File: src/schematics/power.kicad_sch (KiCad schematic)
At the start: 43 parts, among them U1 L6981NDR, U2 L6981NDR, U3 ST1S41PHR, U4 L6981NDR, U5 LM3880

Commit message: Adds footprint for etq-p5m220yfc (#64)
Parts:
- L2, L4: footprint (none) -> ECAP5-DPROC:ETQ-P5M220YFC
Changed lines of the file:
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@@
 			)
 		)
-		(property "Footprint" ""
+		(property "Footprint" "ECAP5-DPROC:ETQ-P5M220YFC"
 			(at 240.03 34.29 0)
 			(effects
@@
 			)
 		)
-		(property "Footprint" ""
+		(property "Footprint" "ECAP5-DPROC:ETQ-P5M220YFC"
 			(at 240.03 85.09 0)
 			(effects

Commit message: Adds footprint for ETQ-P3M2R2KVP (#65)
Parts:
- L3: footprint (none) -> ECAP5-DPROC:ETQ-P3M2R2KVP
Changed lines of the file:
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@@
 			)
 		)
-		(property "Footprint" ""
+		(property "Footprint" "ECAP5-DPROC:ETQ-P3M2R2KVP"
 			(at 104.14 85.09 0)
 			(effects

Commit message: Add footprint for st1s41phr
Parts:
- U3: footprint (none) -> ECAP5-DPROC:ST1S41PHR
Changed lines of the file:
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@@
 			)
 		)
-		(property "Footprint" ""
+		(property "Footprint" "ECAP5-DPROC:ST1S41PHR"
 			(at 88.265 100.33 0)
 			(effects

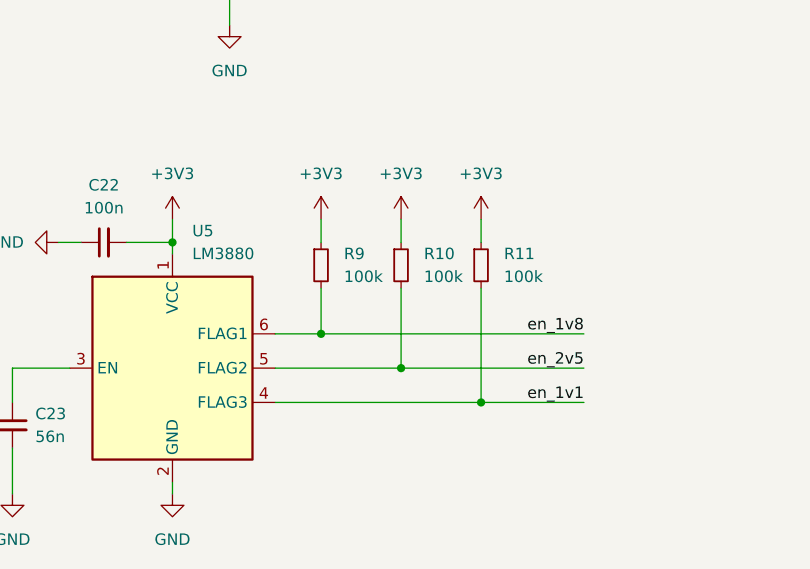
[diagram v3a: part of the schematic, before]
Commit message: Adds footprint for lm3880 (#67)
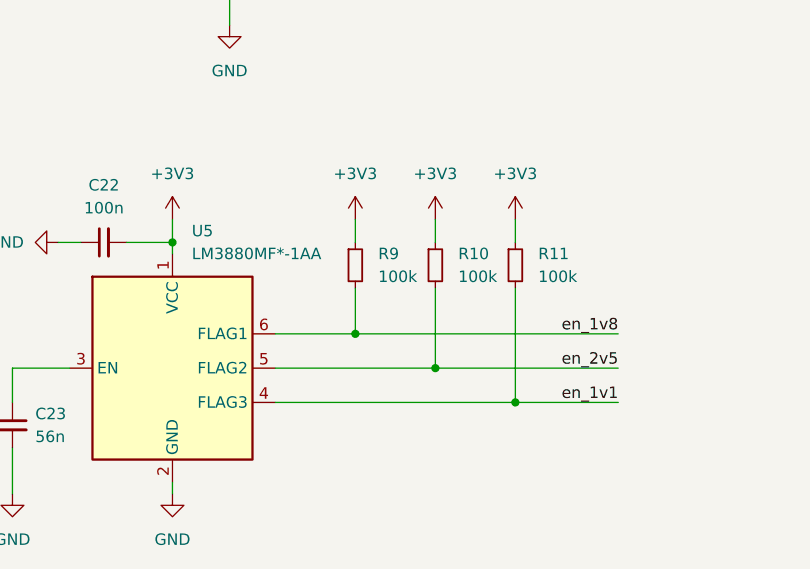
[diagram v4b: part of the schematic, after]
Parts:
- U5: value LM3880 -> LM3880MF*-1AA; footprint (none) -> ECAP5-DPROC:LM3880
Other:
- moved on the sheet: R10, R11, R9

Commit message: Add remaining component footprints (#79)
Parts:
- C1, C13, C14, C2, C22, C23, C3, C4: footprint (none) -> Capacitor_SMD:C_0402_1005Metric
- C11, C12, C16, C20, C21, C8, C9: footprint (none) -> Capacitor_SMD:C_0603_1608Metric
- C5: footprint Capacitor_SMD:C_1210_3225Metric -> Capacitor_SMD:C_0805_2012Metric
- R1, R10, R11, R2, R3, R4, R5, R6, R7, R8, R9: footprint (none) -> Resistor_SMD:R_0603_1608Metric
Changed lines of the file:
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@@
 			)
 		)
-		(property "Footprint" ""
+		(property "Footprint" "Resistor_SMD:R_0603_1608Metric"
 			(at 110.49 90.17 0)
 			(effects
@@
 			)
 		)
-		(property "Footprint" ""
+		(property "Footprint" "Capacitor_SMD:C_0402_1005Metric"
 			(at 60.96 153.67 0)
 			(effects
@@
 			)
 		)
-		(property "Footprint" ""
+		(property "Footprint" "Resistor_SMD:R_0603_1608Metric"
 			(at 250.19 90.17 0)
 			(effects
@@
 			)
 		)
-		(property "Footprint" ""
+		(property "Footprint" "Resistor_SMD:R_0603_1608Metric"
 			(at 110.49 100.33 0)
 			(effects
@@
 			)
 		)
-		(property "Footprint" ""
+		(property "Footprint" "Capacitor_SMD:C_0402_1005Metric"
 			(at 246.38 90.17 0)
 			(effects
@@
 			)
 		)
-		(property "Footprint" ""
+		(property "Footprint" "Resistor_SMD:R_0603_1608Metric"
 			(at 250.19 49.53 0)
 			(effects
@@
 			)
 		)
-		(property "Footprint" ""
+		(property "Footprint" "Capacitor_SMD:C_0603_1608Metric"
 			(at 193.04 48.26 0)
 			(effects
@@
 			)
 		)
-		(property "Footprint" ""
+		(property "Footprint" "Resistor_SMD:R_0603_1608Metric"
 			(at 116.84 135.89 0)
 			(effects
@@
 			)
 		)
-		(property "Footprint" ""
+		(property "Footprint" "Capacitor_SMD:C_0603_1608Metric"
 			(at 58.42 95.25 0)
 			(effects
@@
 			)
 		)
-		(property "Footprint" ""
+		(property "Footprint" "Capacitor_SMD:C_0603_1608Metric"
 			(at 64.77 48.26 0)
 			(effects
@@
 			)
 		)
-		(property "Footprint" ""
+		(property "Footprint" "Capacitor_SMD:C_0402_1005Metric"
 			(at 71.12 133.35 0)
 			(effects
@@
 			)
 		)
-		(property "Footprint" ""
+		(property "Footprint" "Capacitor_SMD:C_0603_1608Metric"
 			(at 182.88 48.26 0)
 			(effects
@@
 			)
 		)
-		(property "Footprint" ""
+		(property "Footprint" "Capacitor_SMD:C_0402_1005Metric"
 			(at 229.87 87.63 0)
 			(effects
@@
 			)
 		)
-		(property "Footprint" ""
+		(property "Footprint" "Capacitor_SMD:C_0603_1608Metric"
 			(at 182.88 99.06 0)
 			(effects
@@
 			)
 		)
-		(property "Footprint" ""
+		(property "Footprint" "Resistor_SMD:R_0603_1608Metric"
 			(at 121.92 49.53 0)
 			(effects
@@
 			)
 		)
-		(property "Footprint" ""
+		(property "Footprint" "Capacitor_SMD:C_0603_1608Metric"
 			(at 54.61 48.26 0)
 			(effects
@@
 			)
 		)
-		(property "Footprint" ""
+		(property "Footprint" "Resistor_SMD:R_0603_1608Metric"
 			(at 107.95 135.89 0)
 			(effects
@@
 			)
 		)
-		(property "Footprint" ""
+		(property "Footprint" "Resistor_SMD:R_0603_1608Metric"
 			(at 99.06 135.89 0)
 			(effects
@@
 			)
 		)
-		(property "Footprint" ""
+		(property "Footprint" "Capacitor_SMD:C_0603_1608Metric"
 			(at 193.04 99.06 0)
 			(effects
@@
 			)
 		)
-		(property "Footprint" ""
+		(property "Footprint" "Capacitor_SMD:C_0402_1005Metric"
 			(at 246.38 39.37 0)
 			(effects
@@
 			)
 		)
-		(property "Footprint" ""
+		(property "Footprint" "Resistor_SMD:R_0603_1608Metric"
 			(at 121.92 39.37 0)
 			(effects
@@
 			)
 		)
-		(property "Footprint" ""
+		(property "Footprint" "Resistor_SMD:R_0603_1608Metric"
 			(at 250.19 39.37 0)
 			(effects
@@
 			)
 		)
-		(property "Footprint" ""
+		(property "Footprint" "Capacitor_SMD:C_0402_1005Metric"
 			(at 118.11 39.37 0)
 			(effects
@@
 			)
 		)
-		(property "Footprint" ""
+		(property "Footprint" "Capacitor_SMD:C_0402_1005Metric"
 			(at 229.87 36.83 0)
 			(effects
@@
 			)
 		)
-		(property "Footprint" "Capacitor_SMD:C_1210_3225Metric"
+		(property "Footprint" "Capacitor_SMD:C_0805_2012Metric"
 			(at 133.35 44.45 0)
 			(effects
@@
 			)
 		)
-		(property "Footprint" ""
+		(property "Footprint" "Capacitor_SMD:C_0402_1005Metric"
 			(at 101.6 36.83 0)
 			(effects
@@
 			)
 		)
-		(property "Footprint" ""
+		(property "Footprint" "Resistor_SMD:R_0603_1608Metric"
 			(at 250.19 100.33 0)
 			(effects

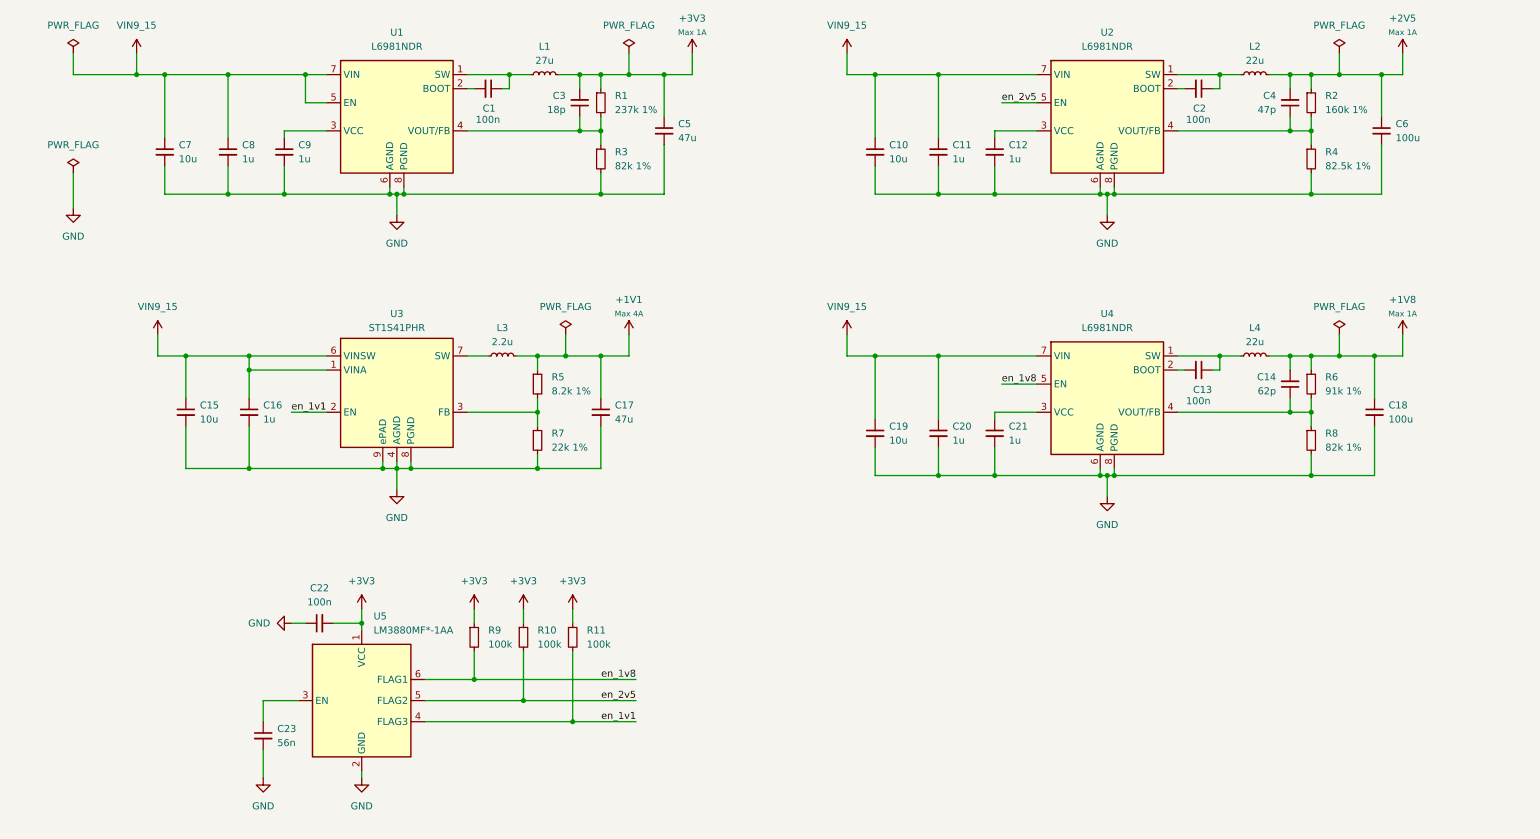
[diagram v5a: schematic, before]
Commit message: Use TI power ICs instead of ST (#81)
* Update big inductors for smaller ones

* Add TI power designer reports for buck converted

* Add schematic for the 1V1 regulator

* Replace the other buck converters

* Add footprints for TI buck converters

* Add remaining footprints

* Update documentation following changes to power schematic
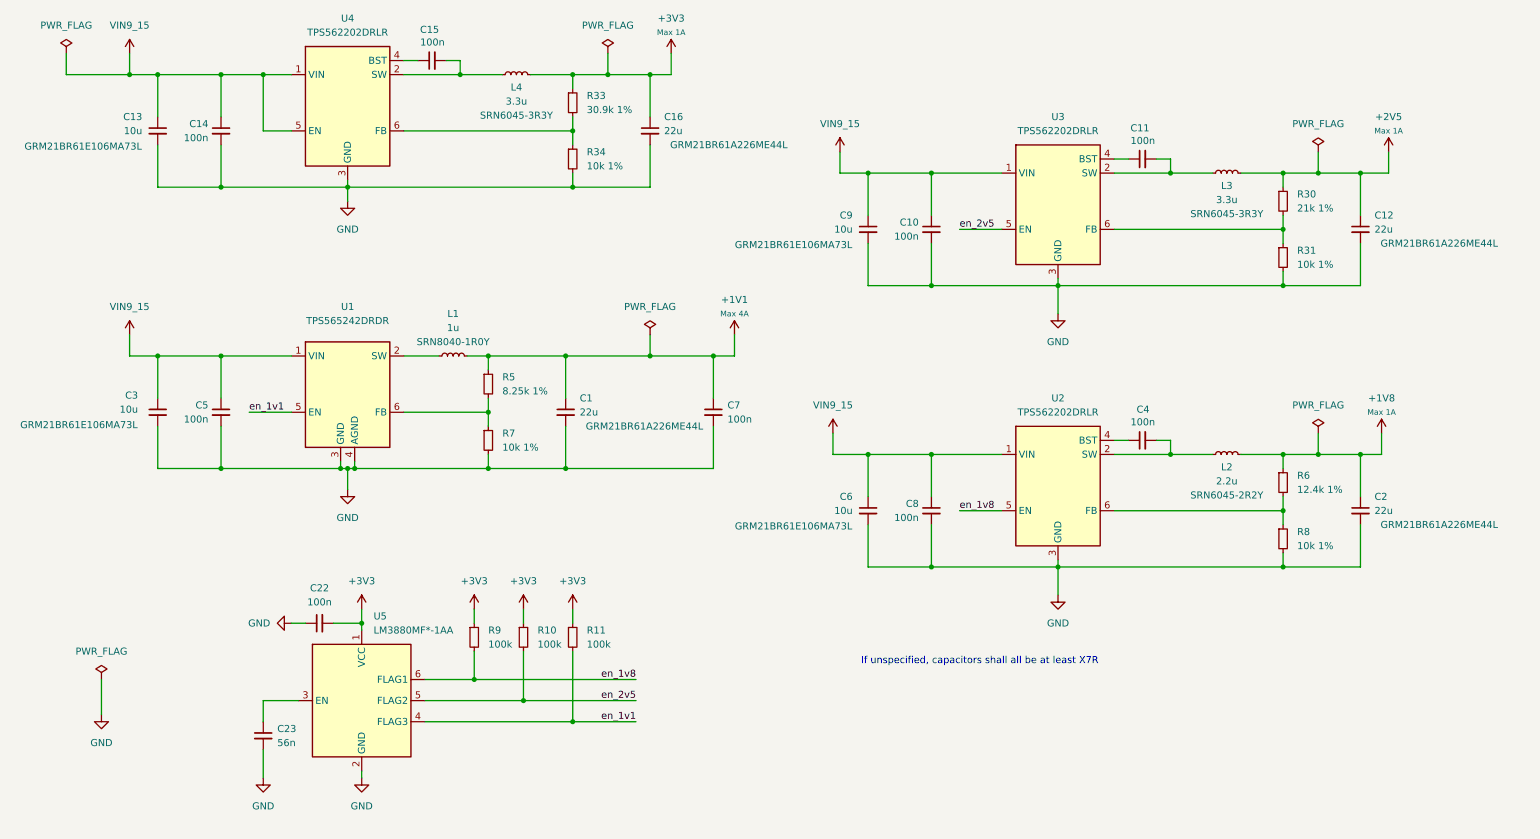
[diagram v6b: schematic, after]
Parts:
- removed C17: 47u, Capacitor_SMD:C_1210_3225Metric, symbol Device:C_Small
- removed C18: 100u, Capacitor_SMD:C_1210_3225Metric, symbol Device:C_Small
- removed C19: 10u, Capacitor_SMD:C_1206_3216Metric, symbol Device:C_Small
- removed C20, C21: 1u, Capacitor_SMD:C_0603_1608Metric, symbol Device:C_Small
- removed R1: 237k 1%, Resistor_SMD:R_0603_1608Metric, symbol Device:R_Small
- removed R2: 160k 1%, Resistor_SMD:R_0603_1608Metric, symbol Device:R_Small
- removed R3: 82k 1%, Resistor_SMD:R_0603_1608Metric, symbol Device:R_Small
- removed R4: 82.5k 1%, Resistor_SMD:R_0603_1608Metric, symbol Device:R_Small
- removed U1, U2, U4: L6981NDR, ECAP5-DPROC:L6981, symbol ECAP5-BSOM:L6981NDR
- removed U3: ST1S41PHR, ECAP5-DPROC:ST1S41PHR, symbol ECAP5-BSOM:ST1S41PHR
- added R30: 21k 1%, Resistor_SMD:R_0402_1005Metric, symbol Device:R_Small
- added R31, R34: 10k 1%, Resistor_SMD:R_0402_1005Metric, symbol Device:R_Small
- added R33: 30.9k 1%, Resistor_SMD:R_0402_1005Metric, symbol Device:R_Small
- added U1: TPS565242DRDR, ECAP5-DPROC:TI_DRL0006A, symbol ECAP5-BSOM:TPS565242DRDR
- added U2, U3, U4: TPS562202DRLR, ECAP5-DPROC:TI_DRL0006A, symbol ECAP5-BSOM:TPS562202DRLR
- C1, C2: value 100n -> 22u; footprint Capacitor_SMD:C_0402_1005Metric -> Capacitor_SMD:C_0805_2012Metric; Part (none) -> GRM21BR61A226ME44L
- C10, C7: value 10u -> 100n; footprint Capacitor_SMD:C_1206_3216Metric -> Capacitor_SMD:C_0603_1608Metric; Component GRM319R61E106KA12D -> (none)
- C11: value 1u -> 100n; footprint Capacitor_SMD:C_0603_1608Metric -> Capacitor_SMD:C_0402_1005Metric
- C12, C16: value 1u -> 22u; footprint Capacitor_SMD:C_0603_1608Metric -> Capacitor_SMD:C_0805_2012Metric; Part (none) -> GRM21BR61A226ME44L
- C13: value 100n -> 10u; footprint Capacitor_SMD:C_0402_1005Metric -> Capacitor_SMD:C_0805_2012Metric; Part (none) -> GRM21BR61E106MA73L
- C14: value 62p -> 100n; footprint Capacitor_SMD:C_0402_1005Metric -> Capacitor_SMD:C_0603_1608Metric
- C15: value 10u -> 100n; footprint Capacitor_SMD:C_1206_3216Metric -> Capacitor_SMD:C_0402_1005Metric; Component GRM319R61E106KA12D -> (none)
- C3: value 18p -> 10u; footprint Capacitor_SMD:C_0402_1005Metric -> Capacitor_SMD:C_0805_2012Metric; Part (none) -> GRM21BR61E106MA73L
- C4: value 47p -> 100n
- C5: value 47u -> 100n; footprint Capacitor_SMD:C_0805_2012Metric -> Capacitor_SMD:C_0603_1608Metric; Component 12106D476MAT2A -> (none)
- C6: value 100u -> 10u; footprint Capacitor_SMD:C_1210_3225Metric -> Capacitor_SMD:C_0805_2012Metric; Component GRM32ER60J107ME20L -> (none); Part (none) -> GRM21BR61E106MA73L
- C8: value 1u -> 100n
- C9: value 1u -> 10u; footprint Capacitor_SMD:C_0603_1608Metric -> Capacitor_SMD:C_0805_2012Metric; Part (none) -> GRM21BR61E106MA73L
- L1: value 27u -> 1u; footprint ECAP5-DPROC:744770127 -> ECAP5-DPROC:Bourns_SRN8040; Component 744770127 -> (none); Part (none) -> SRN8040-1R0Y
- L2: value 22u -> 2.2u; footprint ECAP5-DPROC:ETQ-P5M220YFC -> ECAP5-DPROC:Bourns_SRN6045; Component ETQ-P5M220YFC -> (none); Part (none) -> SRN6045-2R2Y
- L3: value 2.2u -> 3.3u; footprint ECAP5-DPROC:ETQ-P3M2R2KVP -> ECAP5-DPROC:Bourns_SRN6045; Component ETQ-P3M2R2KVP -> (none); Part (none) -> SRN6045-3R3Y
- L4: value 22u -> 3.3u; footprint ECAP5-DPROC:ETQ-P5M220YFC -> ECAP5-DPROC:Bourns_SRN6045; Component ETQ-P5M220YFC -> (none); Part (none) -> SRN6045-3R3Y
- R10, R11, R9: footprint Resistor_SMD:R_0603_1608Metric -> Resistor_SMD:R_0402_1005Metric
- R5: value 8.2k 1% -> 8.25k 1%; footprint Resistor_SMD:R_0603_1608Metric -> Resistor_SMD:R_0402_1005Metric
- R6: value 91k 1% -> 12.4k 1%; footprint Resistor_SMD:R_0603_1608Metric -> Resistor_SMD:R_0402_1005Metric
- R7: value 22k 1% -> 10k 1%; footprint Resistor_SMD:R_0603_1608Metric -> Resistor_SMD:R_0402_1005Metric
- R8: value 82k 1% -> 10k 1%; footprint Resistor_SMD:R_0603_1608Metric -> Resistor_SMD:R_0402_1005Metric
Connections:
- net +1V1: now also C1.1, C7.1, L1.2; no longer L3.2
- net +1V8: now also C2.1, L2.2; no longer C14.2, L4.2
- net +2V5: now also C12.1, L3.2, R30.1; no longer C4.2, C6.1, L2.2
- net +3V3: now also C16.1, L4.2, R33.1; no longer C3.2, C5.1, L1.2
- net GND: now also C1.2, C13.2, C14.2, C2.2, C3.2, R31.2, R34.2, U1.3 (GND), U1.4 (AGND), U2.3 (GND), U3.3 (GND), U4.3 (GND); no longer C11.2, C15.2
- net VIN9_15: now also C13.1, C14.1, C3.1, C5.1, C6.1, C9.1, U1.1 (VIN), U2.1 (VIN), U3.1 (VIN), U4.1 (VIN), U4.5 (EN); no longer C11.1, C15.1, C16.1, C7.1
- net en_1v1: now also U1.5 (EN)
- net en_1v8: now also U2.5 (EN)
- net en_2v5: now also U3.5 (EN)
- net at R5.2, R7.1: now also U1.6 (FB)
- net at L3.1: now also C11.2, U3.2 (SW)
- net at L1.1: now also U1.2 (SW); no longer C1.1
- net at R6.2, R8.1: now also U2.6 (FB); no longer C14.1
- net at L4.1: now also C15.2, U4.2 (SW); no longer C13.1
- net at C4.1: now also U2.4 (BST)
- net at L2.1: now also C4.2, U2.2 (SW); no longer C2.1
- new net: C15.1, U4.4 (BST)
- new net: R33.2, R34.1, U4.6 (FB)
- new net: R30.2, R31.1, U3.6 (FB)
- new net: C11.1, U3.4 (BST)
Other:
- note added: "If unspecified, capacitors shall all be at least X7R"
- moved on the sheet: R5, R7
